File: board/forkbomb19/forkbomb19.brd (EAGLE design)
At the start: 89.2 x 57 mm, 66 parts, among them SW1 SPST_TACT-KMR2, T3 MMUN2133LT1G, U1 ESP-WROOM-03, U4 TPS61090RSAR, U5 MCP73871, X3 POT_GND, X4 POT_3V3, X5 POT_SIG

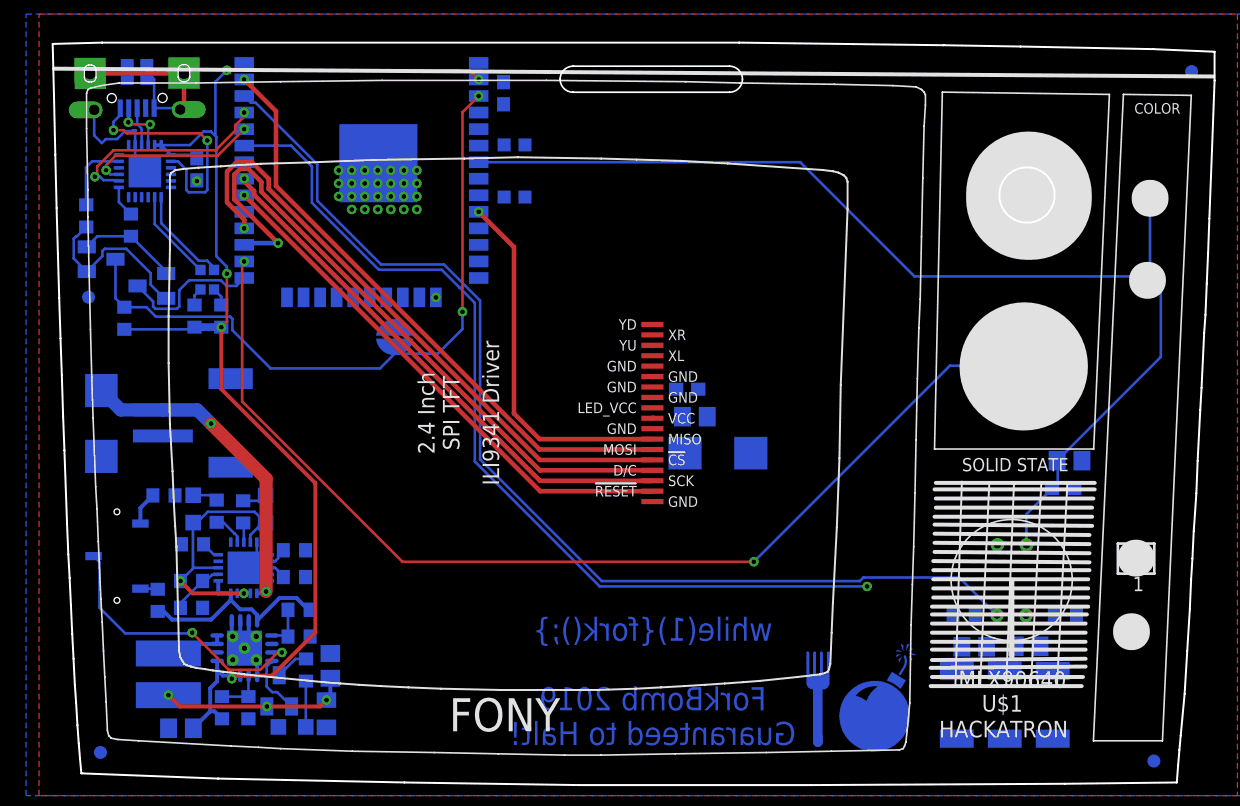
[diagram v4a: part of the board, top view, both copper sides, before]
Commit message: footprint pretty much done, needs cleanup
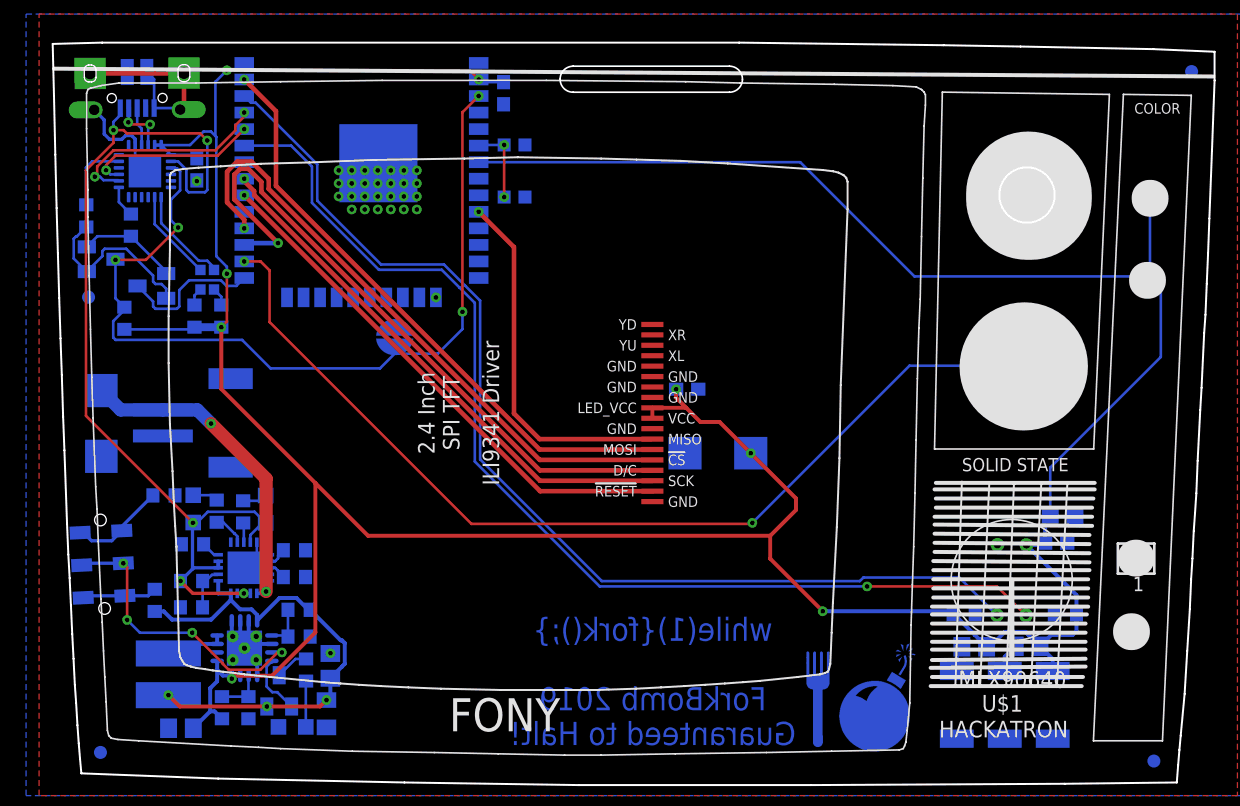
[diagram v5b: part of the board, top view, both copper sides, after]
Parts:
- removed C8: 10uF, resistor:C0805
- removed U$17: CL-SB-12A-02T, defcon:CL-SB-12A-02T
- added U$8: JS202011JAQN, forkbomb19:JS202011JAQN
- moved C12 4.30 mm to (76.6, 20.4)
- moved C11 4.22 mm to (76.1, 18.4)
- moved R18 0.23 mm to (6.88, 14.0)
- turned R26 to 0 degrees
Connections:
- removed net +5V: U3.8, X1.VBUS
- net +3V3: no longer C8.1
- net ENABLE: now also U$8.P$2, U$8.P$5; no longer U$17.P$2
- net GND: no longer C8.2
- net N$13: now also U$8.P$3, U$8.P$6; no longer U$17.P$1
- net N$42: now also U$8.P$1, U$8.P$4; no longer U$17.P$3
- net VBUS: now also U3.8, X1.VBUS
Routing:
- net +3V3: track 131.3 -> 230.7 mm, vias 5 -> 8
- net VBUS: track 21.5 -> 74.4 mm, vias 2 -> 5
- net +5V: track 18.0 -> 0.00 mm, vias 2 -> 0
- net I2C_SDA: track 70.6 -> 85.9 mm
- net EN: track 52.0 -> 65.6 mm, vias 2 -> 4
- net VBAT: track 31.9 -> 38.7 mm
- net TOUCH1: track 82.4 -> 75.9 mm, vias 4 -> 3
- net N$2: track 0.00 -> 5.98 mm, vias 0 -> 2
- net N$13: track 2.55 -> 7.48 mm
- net N$42: track 1.35 -> 5.76 mm
- net N$31: track 0.00 -> 2.23 mm
- net N$12: track 0.00 -> 2.02 mm
- net I2C_SCL: track 83.3 -> 85.0 mm
- net N$28: track 4.17 -> 3.44 mm
- net ENABLE: track 22.1 -> 22.5 mm, vias 2 -> 4
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
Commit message: small cleanup
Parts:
- removed HRDRST: (no value), SparkFun-Jumpers:SMT-JUMPER_2_NO_SILK_ROUND
- added SW2: SPST_TACT-KMR2, adafruit:KMR2
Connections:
- net EN: now also SW2.2, SW2.4; no longer HRDRST.2
- net GND: now also SW2.1, SW2.3; no longer HRDRST.1
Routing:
- net EN: track 65.6 -> 60.7 mm
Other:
- board text added: "Soft Rst"

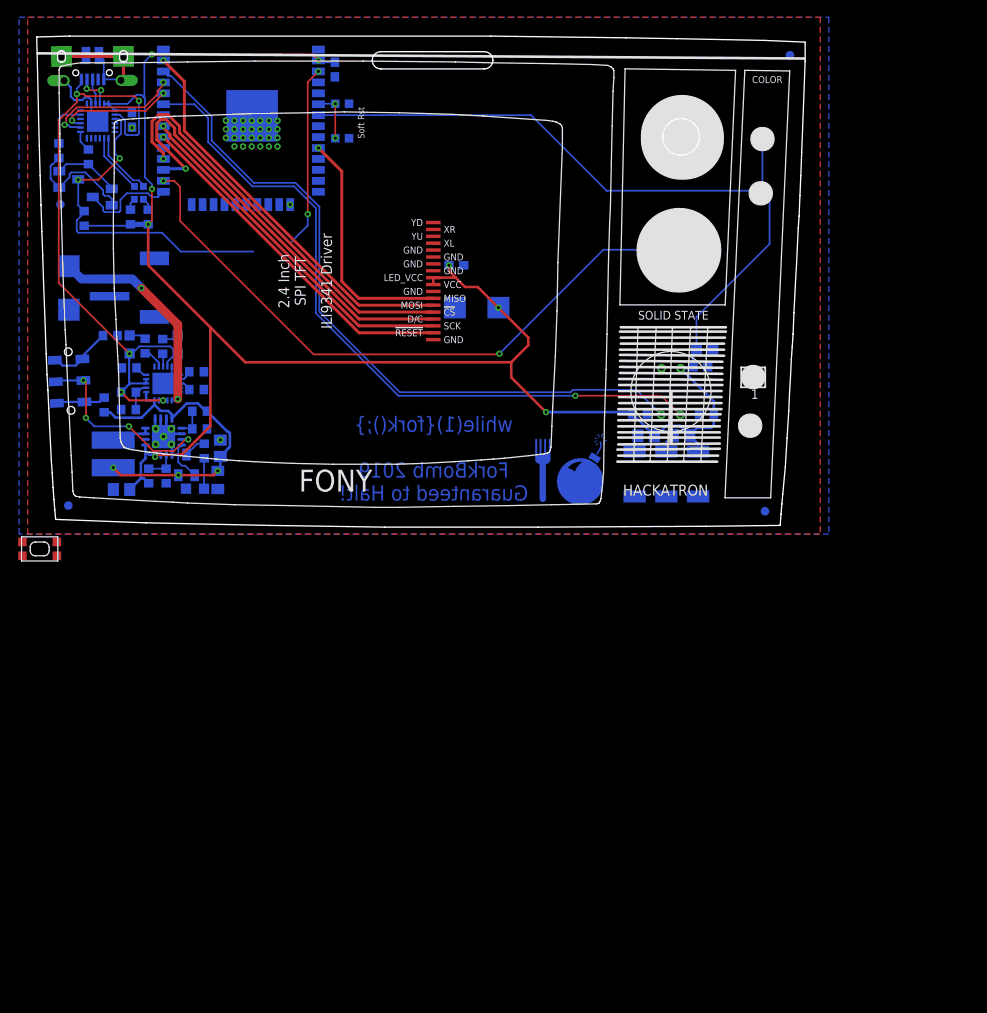
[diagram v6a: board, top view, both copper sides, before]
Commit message: made a BOM, cleaned up the board, added a styles 27 button
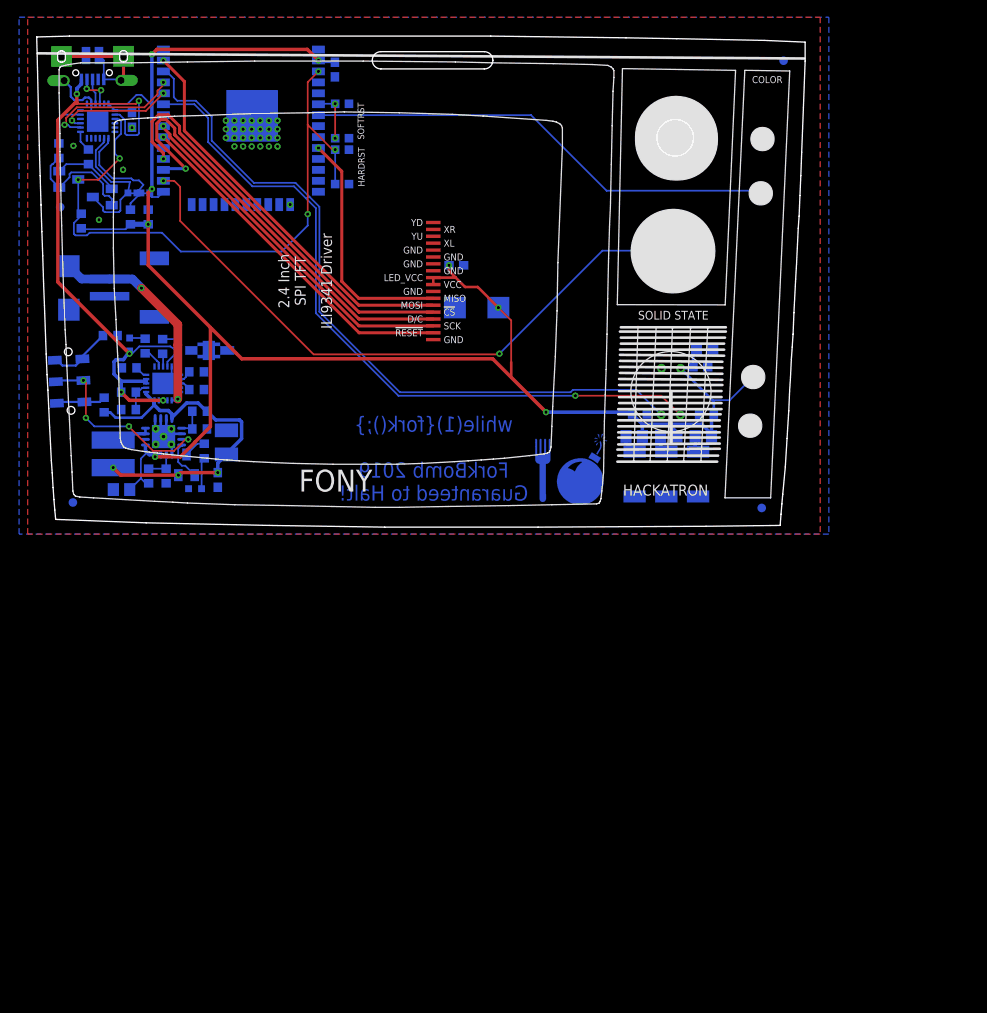
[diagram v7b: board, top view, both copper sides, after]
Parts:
- removed CHRG/LBO: ORANGE, microbuilder:CHIPLED_0805_NOOUTLINE
- removed LED1: RED, microbuilder:CHIPLED_0805_NOOUTLINE
- removed SW1, SW2: SPST_TACT-KMR2, adafruit:KMR2
- added CHRG: ORANGE, led:CHIP-LED0603
- added HARDRST, SOFTRESET: SPST_TACT-KMR2, adafruit:KMR2
- added LOW_BATT: RED, led:CHIP-LED0603
- added R3: 0, resistor:R0805
- C16: value 0.1uF -> 100nF; device microbuilder:0805_10MGAP -> rcl:C0603
- C2: device microbuilder:0805-NO -> rcl:C1210
- DONE: device microbuilder:CHIPLED_0805_NOOUTLINE -> led:CHIP-LED0603
- RX, TX: device led:SML0603 -> led:CHIP-LED0603
- T1, T2: device transistor-neu-to92:SOT23-BEC -> transistor:SOT23-BEC
- moved X3 27.7 mm to (83.3, 44.9), flipped to the bottom
- moved X4 27.6 mm to (82.2, 17.2)
- moved R8 1.48 mm to (72.4, 10.3)
- moved R22 1.39 mm to (68.4, 10.3)
- moved C2 0.99 mm to (21.1, 9.65)
- moved FID3 0.97 mm to (85.7, 54.0)
- moved C3 0.69 mm to (74.0, 31.9)
- moved TOUCH 0.69 mm to (72.9, 31.8)
- moved FID1 0.64 mm to (3.25, 2.67)
- moved FID2 0.54 mm to (83.2, 2.04)
- moved R1 0.45 mm to (4.22, 35.3)
- moved FID4 0.31 mm to (1.77, 37.0)
- renumbered L2 to L1
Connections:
- new net N$7: LOGO_B.1, R3.2
- net +3V3: now also R3.1; no longer LOGO_B.1
- net EN: now also HARDRST.2, HARDRST.4; no longer SW2.2, SW2.4
- net GND: now also HARDRST.1, HARDRST.3, LOW_BATT.C, SOFTRESET.2, SOFTRESET.4; no longer LED1.C, SW1.2, SW1.4, SW2.1, SW2.3
- net N$2: now also SOFTRESET.1, SOFTRESET.3; no longer SW1.1, SW1.3
- net N$24: now also LOW_BATT.A; no longer LED1.A
- net N$36: now also CHRG.C; no longer CHRG/LBO.C
- net VBUS: now also CHRG.A; no longer CHRG/LBO.A
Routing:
- net EN: track 60.7 -> 74.9 mm, vias 4 -> 5
- net +3V3: track 230.7 -> 242.4 mm
- net VBAT: track 38.7 -> 44.9 mm
- net N$19: track 7.65 -> 10.8 mm
- net VBUS: track 74.4 -> 77.2 mm
- net N$20: track 7.04 -> 9.67 mm
- net N$7: track 0.00 -> 1.91 mm
- net I2C_SCL: track 85.0 -> 86.3 mm
- net N$16: track 4.70 -> 5.90 mm
- net N$21: track 1.38 -> 2.44 mm
- net TOUCH1: track 75.9 -> 75.2 mm
- net N$22: track 1.43 -> 1.96 mm
- net GND: vias 30 -> 32
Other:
- outline, holes or cut-outs redrawn
- board text added: "HARDRST"
- board text added: "POT_GND"
- board text added: "SOFTRST"
- board text removed: "Soft Rst"

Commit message: cleaning up board and schematic
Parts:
- removed C3: (no value), resistor:C0805
- added FRAME1: FRAME-LEDGER, SparkFun-Aesthetics:CREATIVE_COMMONS
- added LOGO1: OSHW-LOGOS-COPPER, SparkFun-Aesthetics:OSHW-LOGO-S_COPPER
- moved TX 0.36 mm to (10.0, 38.6), turned to 0 degrees
- moved RX 0.05 mm to (11.4, 38.6), turned to 0 degrees
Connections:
- net TOUCH1: no longer C3.1, TOUCH.P$1
- net TOUCH2: now also TOUCH.P$1
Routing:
- net TOUCH1: track 75.2 -> 0.00 mm, vias 3 -> 0
- net TOUCH2: track 0.00 -> 74.7 mm, vias 0 -> 3
- net +3V3: track 242.4 -> 225.0 mm
- net N$21: track 2.44 -> 1.21 mm
- net N$19: track 10.8 -> 9.78 mm
- net N$20: track 9.67 -> 8.79 mm
- net N$22: track 1.96 -> 1.44 mm
- net GND: vias 32 -> 33
